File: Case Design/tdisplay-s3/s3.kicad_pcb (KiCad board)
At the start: 2 copper layers, 34 x 109.7 mm, 10 parts, among them SW6 SW_PUSH_6mm_H9.5mm, SW7 SW_PUSH_6mm_H9.5mm, SW8 SW_PUSH_6mm_H9.5mm

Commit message: change led to 5mm and add transistor to it
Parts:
- removed 3MM IR LED: LED_D3.0mm_Clear, LED_THT:LED_D3.0mm_Clear
- added 2.5ohm: R_Axial_DIN0204_L3.6mm_D1.6mm_P5.08mm_Horizontal, Resistor_THT:R_Axial_DIN0204_L3.6mm_D1.6mm_P5.08mm_Horizontal, F.Cu at (198.8, 61.6)
- added 3.3ohm: R_Axial_DIN0204_L3.6mm_D1.6mm_P5.08mm_Horizontal, Resistor_THT:R_Axial_DIN0204_L3.6mm_D1.6mm_P5.08mm_Horizontal, F.Cu at (202.6, 61.6)
- added 5MM IR LED: LED_D5.0mm_Clear, LED_THT:LED_D5.0mm_Clear, F.Cu at (208.8, 44.9)
- added NPN: TO-92L_HandSolder, Package_TO_SOT_THT:TO-92L_HandSolder, F.Cu at (205.7, 52.1)
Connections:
- TDisplayS3 pad 5v: (no net) -> 5v
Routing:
- net 5v: track 0.00 -> 11.5 mm
- net irled: track 41.6 -> 30.3 mm
- net ground2: track 32.9 -> 31.0 mm

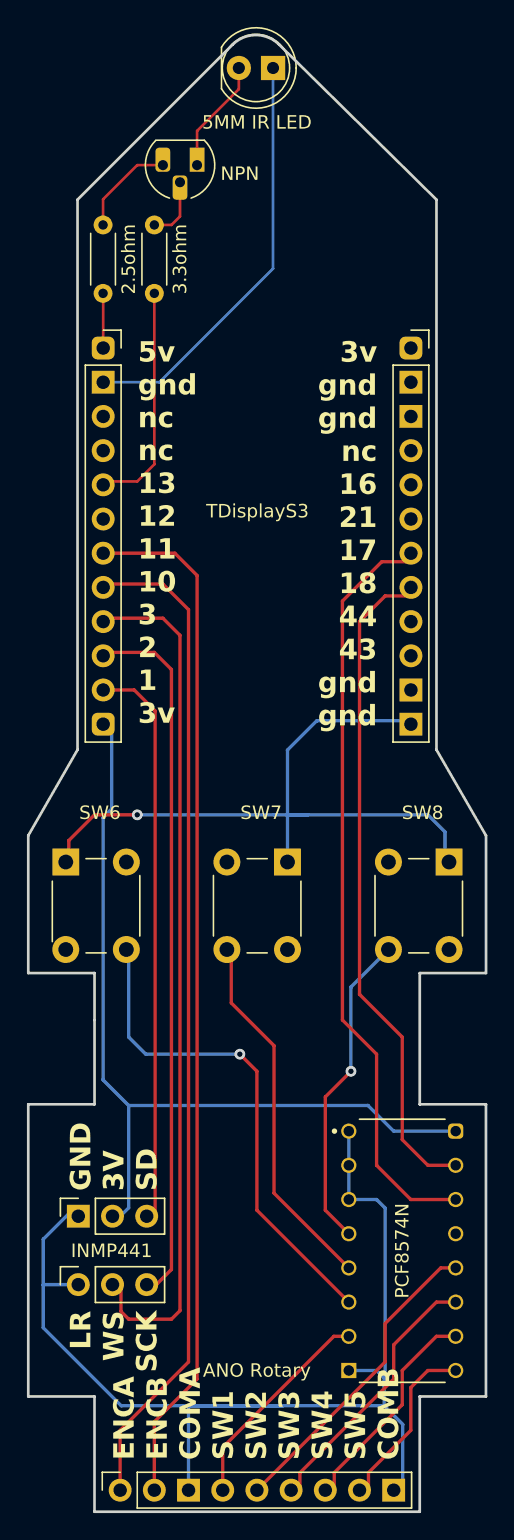
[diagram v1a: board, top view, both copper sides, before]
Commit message: fix ground not connecting to bottom pin
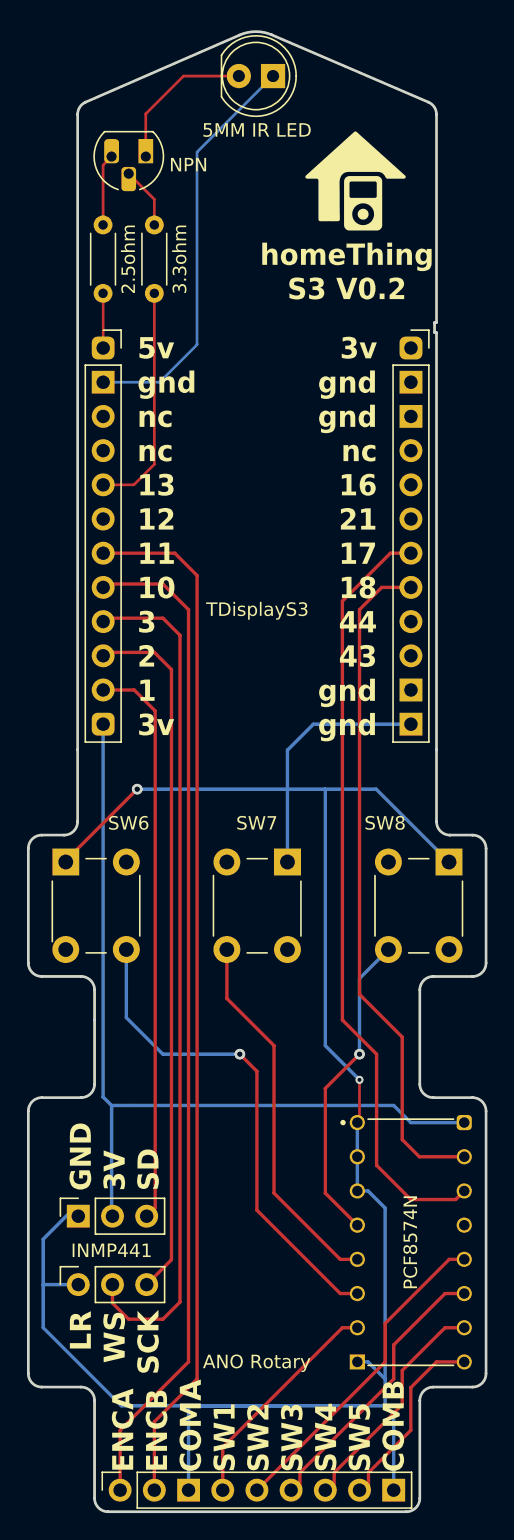
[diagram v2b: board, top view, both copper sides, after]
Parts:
- moved NPN 3.86 mm to (201.9, 51.4)
- moved PCF8574N 0.90 mm to (221.6, 132.1)
- moved 5MM IR LED 0.60 mm to (208.8, 45.5)
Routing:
- net ground: track 142.9 -> 166.8 mm, vias 1 -> 2
- net irled: track 30.3 -> 33.0 mm
- net 5v: track 11.5 -> 9.41 mm
- net SCL: track 57.3 -> 58.2 mm
- net sw3: track 19.5 -> 20.4 mm
- net sw2: track 23.3 -> 24.2 mm
- net sw4: track 16.0 -> 16.9 mm
- net sw1: track 16.2 -> 17.1 mm
- net sw5: track 12.7 -> 13.6 mm
- net SDA: track 50.3 -> 51.2 mm
- net sw7: track 26.9 -> 27.8 mm
- net 3v: track 62.9 -> 63.6 mm
- net ground2: track 31.0 -> 30.4 mm
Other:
- board size 34 x 109.7 mm -> 34 x 109.9 mm
- board text added: "homeThing S3 V0.2"

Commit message: add capacitor to i2c
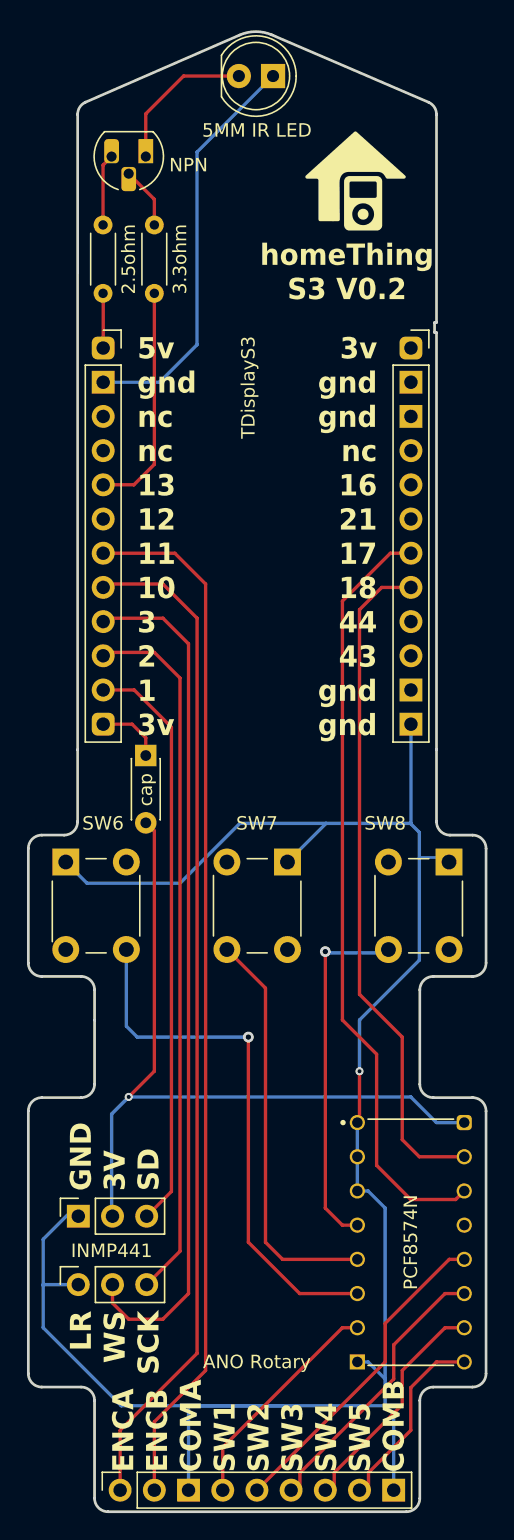
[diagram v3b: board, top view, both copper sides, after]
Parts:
- added cap: C_Disc_D4.3mm_W1.9mm_P5.00mm, Capacitor_THT:C_Disc_D4.3mm_W1.9mm_P5.00mm, F.Cu at (201.9, 95.9)
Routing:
- net ground: track 166.8 -> 153.0 mm, vias 2 -> 1
- net sw8: track 23.4 -> 26.8 mm
- net sw6: track 36.8 -> 40.0 mm
- net sw7: track 27.8 -> 30.3 mm
- net 3v: track 63.6 -> 61.4 mm, vias 0 -> 1
- net sd: track 42.3 -> 43.3 mm
- net SDA: track 51.2 -> 50.3 mm
- net SCL: track 58.2 -> 57.4 mm
- net enca: track 74.7 -> 75.3 mm
- net ws: track 62.6 -> 63.1 mm
- net sck: track 51.5 -> 52.0 mm
- net encb: track 76.9 -> 77.4 mm

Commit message: update cap to be between 3v and gnd for i2c
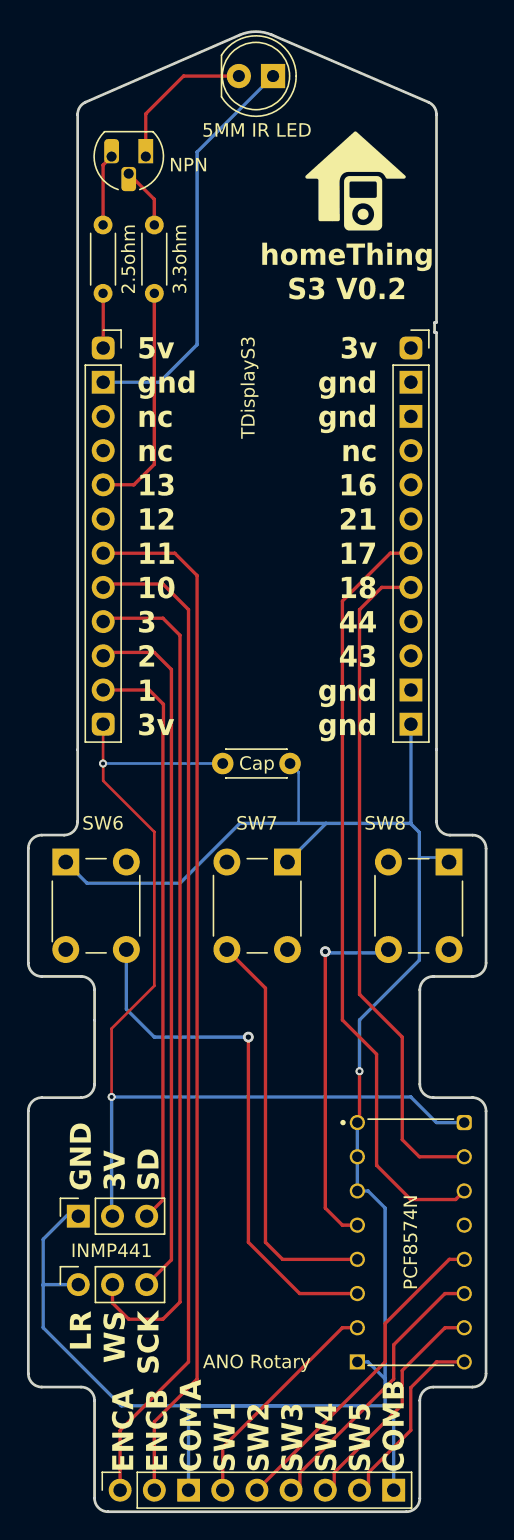
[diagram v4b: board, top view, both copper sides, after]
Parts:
- removed cap: C_Disc_D4.3mm_W1.9mm_P5.00mm, Capacitor_THT:C_Disc_D4.3mm_W1.9mm_P5.00mm
- added Cap: C_Disc_D4.3mm_W1.9mm_P5.00mm, Capacitor_THT:C_Disc_D4.3mm_W1.9mm_P5.00mm, F.Cu at (207.6, 96.5)
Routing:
- net 3v: track 61.4 -> 75.3 mm, vias 1 -> 2
- net ground: track 153.0 -> 157.8 mm
- net sw6: track 40.0 -> 39.3 mm
- net enca: track 75.3 -> 74.7 mm
- net ws: track 63.1 -> 62.6 mm
- net sck: track 52.0 -> 51.5 mm
- net encb: track 77.4 -> 76.9 mm
